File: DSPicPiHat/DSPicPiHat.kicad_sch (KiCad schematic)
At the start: 88 parts, among them J10 Nice!View, J4 Conn_PIC_ICSP_ICD, J5 USB_C_Receptacle_USB2.0, J6 PowerInput, J7 GenericSPIconn, J8 RasPiHeaders, J9 GeneralSPIDisplay, SW1 POWER_Select, SW2 SW_DIP_x08, U1 DSPIC33CH512MP508T-I_PT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

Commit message: Power, USB, and UART
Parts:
- F1: footprint (none) -> Fuse:Fuse_2920_7451Metric
- FB1: footprint (none) -> Resistor_SMD:R_1206_3216Metric
- renumbered Connector_X to Connector_X1, Connector_Y to Connector_Y1, Connector_Z to Connector_Z1
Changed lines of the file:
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@@
     (property "Reference" "F1" (id 0) (at 364.49 186.69 90))
     (property "Value" "3.5 A(?)" (id 1) (at 364.49 189.23 90))
-    (property "Footprint" "" (id 2) (at 369.57 191.77 0)
+    (property "Footprint" "Fuse:Fuse_2920_7451Metric" (id 2) (at 369.57 191.77 0)
       (effects (font (size 1.27 1.27)) (justify left) hide)
     )
@@
   (symbol (lib_id "Connector_Generic:Conn_01x10") (at 92.71 203.2 0) (unit 1)
     (in_bom yes) (on_board yes) (fields_autoplaced)
-    (property "Reference" "Connector_Y" (id 0) (at 95.25 203.1999 0)
+    (property "Reference" "Connector_Y1" (id 0) (at 95.25 203.1999 0)
       (effects (font (size 1.27 1.27)) (justify left))
     )
@@
     (property "Reference" "FB1" (id 0) (at 351.7519 186.69 90))
     (property "Value" "FerriteBead_Small" (id 1) (at 351.7519 189.23 90))
-    (property "Footprint" "" (id 2) (at 351.79 194.818 90)
+    (property "Footprint" "Resistor_SMD:R_1206_3216Metric" (id 2) (at 351.79 194.818 90)
       (effects (font (size 1.27 1.27)) hide)
     )
@@
   (symbol (lib_id "Connector_Generic:Conn_01x10") (at 35.56 203.2 0) (unit 1)
     (in_bom yes) (on_board yes) (fields_autoplaced)
-    (property "Reference" "Connector_X" (id 0) (at 38.1 203.1999 0)
+    (property "Reference" "Connector_X1" (id 0) (at 38.1 203.1999 0)
       (effects (font (size 1.27 1.27)) (justify left))
     )
@@
   (symbol (lib_id "Connector_Generic:Conn_01x10") (at 149.86 203.2 0) (unit 1)
     (in_bom yes) (on_board yes) (fields_autoplaced)
-    (property "Reference" "Connector_Z" (id 0) (at 152.4 203.1999 0)
+    (property "Reference" "Connector_Z1" (id 0) (at 152.4 203.1999 0)
       (effects (font (size 1.27 1.27)) (justify left))
     )
@@
     )
     (path "/a11b1377-8e72-4336-93fb-5d9a6c63e6db"
-      (reference "Connector_X") (unit 1) (value "Conn_01x10") (footprint "Connector_Molex:Molex_Micro-Fit_3.0_43045-1012_2x05_P3.00mm_Vertical")
+      (reference "Connector_X1") (unit 1) (value "Conn_01x10") (footprint "Connector_Molex:Molex_Micro-Fit_3.0_43045-1012_2x05_P3.00mm_Vertical")
     )
     (path "/105a757e-8759-4672-9bee-7cf903751d82"
-      (reference "Connector_Y") (unit 1) (value "Conn_01x10") (footprint "Connector_Molex:Molex_Micro-Fit_3.0_43045-1012_2x05_P3.00mm_Vertical")
+      (reference "Connector_Y1") (unit 1) (value "Conn_01x10") (footprint "Connector_Molex:Molex_Micro-Fit_3.0_43045-1012_2x05_P3.00mm_Vertical")
     )
     (path "/d54e99c0-c1b6-49ce-91c0-733d0cf7acf7"
-      (reference "Connector_Z") (unit 1) (value "Conn_01x10") (footprint "Connector_Molex:Molex_Micro-Fit_3.0_43045-1012_2x05_P3.00mm_Vertical")
+      (reference "Connector_Z1") (unit 1) (value "Conn_01x10") (footprint "Connector_Molex:Molex_Micro-Fit_3.0_43045-1012_2x05_P3.00mm_Vertical")
     )
     (path "/455a802c-8183-4f02-bd06-7b17205bfbf6"
@@
     )
     (path "/0b60c446-5161-421b-a91b-bda5e4f17126"
-      (reference "F1") (unit 1) (value "3.5 A(?)") (footprint "")
+      (reference "F1") (unit 1) (value "3.5 A(?)") (footprint "Fuse:Fuse_2920_7451Metric")
     )
     (path "/73568451-6492-491a-bea8-1d81af82b417"
-      (reference "FB1") (unit 1) (value "FerriteBead_Small") (footprint "")
+      (reference "FB1") (unit 1) (value "FerriteBead_Small") (footprint "Resistor_SMD:R_1206_3216Metric")
     )
     (path "/5662e14b-7d70-457a-a9d1-e3f8a620952f"

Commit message: Connected all the coil driver connectors. Added more footprints.
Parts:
- L1: footprint (none) -> Inductor_SMD:L_0805_2012Metric
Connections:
- net EXT_ADC_X_00: now also U1.5 (RC12); no longer U1.6 (RC13)
- net EXT_ADC_X_01: now also U1.6 (RC13); no longer U1.7 (RC14)
- net EXT_ADC_X_02: now also U1.7 (RC14); no longer U1.8 (RC15)
- net EXT_ADC_X_03: now also U1.8 (RC15); no longer U1.15 (RC0)
- net EXT_ADC_Y_00: now also U1.29 (RC2); no longer U1.41 (RB2)
- net EXT_ADC_Y_01: now also U1.30 (RC6); no longer U1.43 (RB3)
- net EXT_ADC_Y_02: now also U1.33 (RC3); no longer U1.45 (RB4)
- net EXT_ADC_Y_03: now also U1.40 (RC7); no longer U1.46 (RC8)
- net EXT_ADC_Z_00: now also U1.45 (RB4); no longer U1.63 (RC4)
- net EXT_ADC_Z_01: now also U1.46 (RC8); no longer U1.65 (RC5)
- net EXT_ADC_Z_02: now also U1.47 (RC9); no longer U1.66 (RC10)
- net EXT_ADC_Z_03: now also U1.52 (RD7); no longer U1.67 (RC11)
- net EXT_X_PWM_01: now also U1.3 (RB15); no longer U1.74 (RD0)
- net EXT_Y_PWM_00: now also U1.15 (RC0); no longer U1.3 (RB15)
- net EXT_Y_PWM_01: now also U1.28 (RC1); no longer U1.73 (RD1)
- net EXT_Z_PWM_00: now also U1.41 (RB2); no longer U1.5 (RC12)
- net EXT_Z_PWM_01: now also U1.43 (RB3); no longer U1.72 (RD2)

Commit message: PCB mostly routed
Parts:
- removed J10: Nice!View, Connector_PinSocket_2.54mm:PinSocket_1x05_P2.54mm_Vertical, symbol Connector:Conn_01x05_Female
- removed J7: GenericSPIconn, Connector_PinSocket_2.54mm:PinSocket_1x08_P2.54mm_Vertical, symbol Connector:Conn_01x08_Female
- removed J9: GeneralSPIDisplay, Connector_PinSocket_2.54mm:PinSocket_1x08_P2.54mm_Vertical, symbol Connector:Conn_01x08_Female
- added J1: Conn_01x09_Female, Connector_PinHeader_2.54mm:PinHeader_1x09_P2.54mm_Vertical, symbol Connector:Conn_01x09_Female
- C13, C14: footprint Capacitor_SMD:C_0805_2012Metric -> Capacitor_SMD:C_0603_1608Metric
- D12, D13, D4, D5: footprint LED_SMD:LED_WS2812B_PLCC4_5.0x5.0mm_P3.2mm -> LED_SMD:LED_WS2812B-2020_PLCC4_2.0x2.0mm
- JP1: footprint (none) -> Connector_PinHeader_2.54mm:PinHeader_1x02_P2.54mm_Vertical
- Y1: footprint (none) -> Crystal:Crystal_SMD_Abracon_ABM10-4Pin_2.5x2.0mm
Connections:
- net AVSS is gone; now on net GND: C12.2, U1.26 (AVSS)
- net GND1 is gone; now on net GND: C2.2, C4.2, C8.2
- net VDD is gone; now on net +3V3: C10.1, C11.1, C6.1, C9.1, L1.2, U1.12 (VDD), U1.31 (VDD), U1.51 (VDD), U1.71 (VDD)
- net VSS is gone; now on net GND: C10.2, C11.2, C6.2, C9.2, U1.11 (VSS), U1.32 (VSS), U1.50 (VSS), U1.70 (VSS)
- net +3V3: now also J1.1 (Pin_1)
- net Backlight: now also J1.9 (Pin_9)
- net DIP_00: no longer U1.16 (RA0)
- net DIP_01: now also U1.65 (RC5); no longer U1.17 (RE2)
- net DIP_02: now also U1.64 (RE13); no longer U1.18 (RA1)
- net DIP_03: now also U1.63 (RC4); no longer U1.19 (RE3)
- net DIP_04: now also U1.62 (RE12); no longer U1.20 (RA2)
- net DIP_05: now also U1.59 (RE11); no longer U1.21 (RA3)
- net DIP_06: now also U1.58 (RB7); no longer U1.22 (RE4)
- net DIP_07: now also U1.57 (RE10); no longer U1.23 (RA4)
- net Data/Command: now also J1.7 (Pin_7)
- net GND: now also J1.2 (Pin_2)
- net PI_CE0: now also U1.73 (RD1); no longer U1.55 (RB5)
- net PI_CE1: now also J1.6 (Pin_6)
- net PI_MISO: now also U1.74 (RD0), J1.3 (Pin_3); no longer U1.75 (RB10)
- net PI_MOSI: now also U1.75 (RB10), J1.4 (Pin_4); no longer U1.56 (RB6)
- net PI_SCLK: now also J1.5 (Pin_5)
- net RST: now also J1.8 (Pin_8)
- net dsPIC_LED_00: now also U1.19 (RE3); no longer U1.36 (RD11)
- net dsPIC_LED_01: now also U1.18 (RA1); no longer U1.37 (RE6)
- net dsPIC_LED_02: now also U1.17 (RE2); no longer U1.38 (RD10)
- net dsPIC_LED_03: now also U1.16 (RA0); no longer U1.39 (RE7)
- net dsPIC_LED_04: now also U1.14 (RD13); no longer U1.42 (RE8)
- net dsPIC_LED_05: now also U1.13 (RD14); no longer U1.44 (RE9)

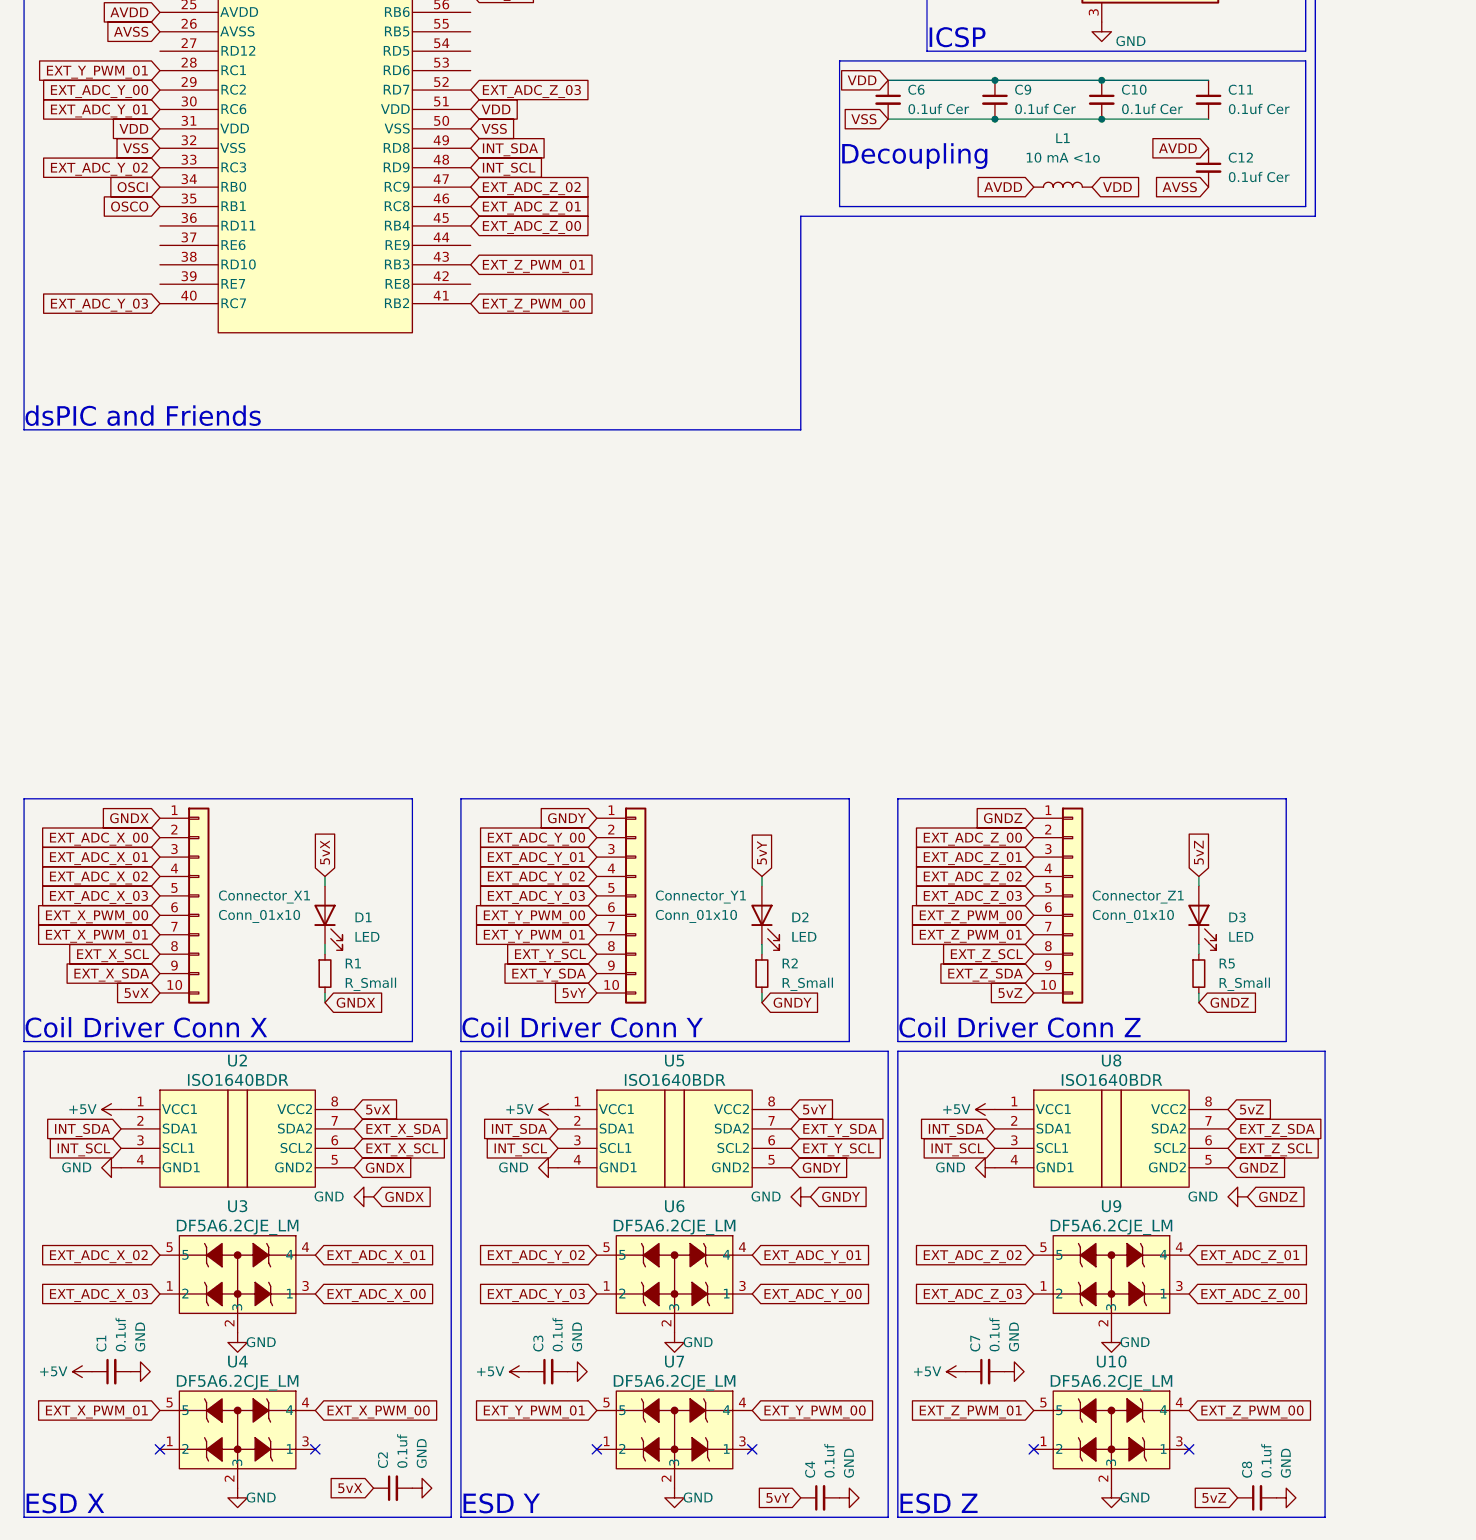
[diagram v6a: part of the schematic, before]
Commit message: changed connectors and removed i2c lines and i2c isolator.
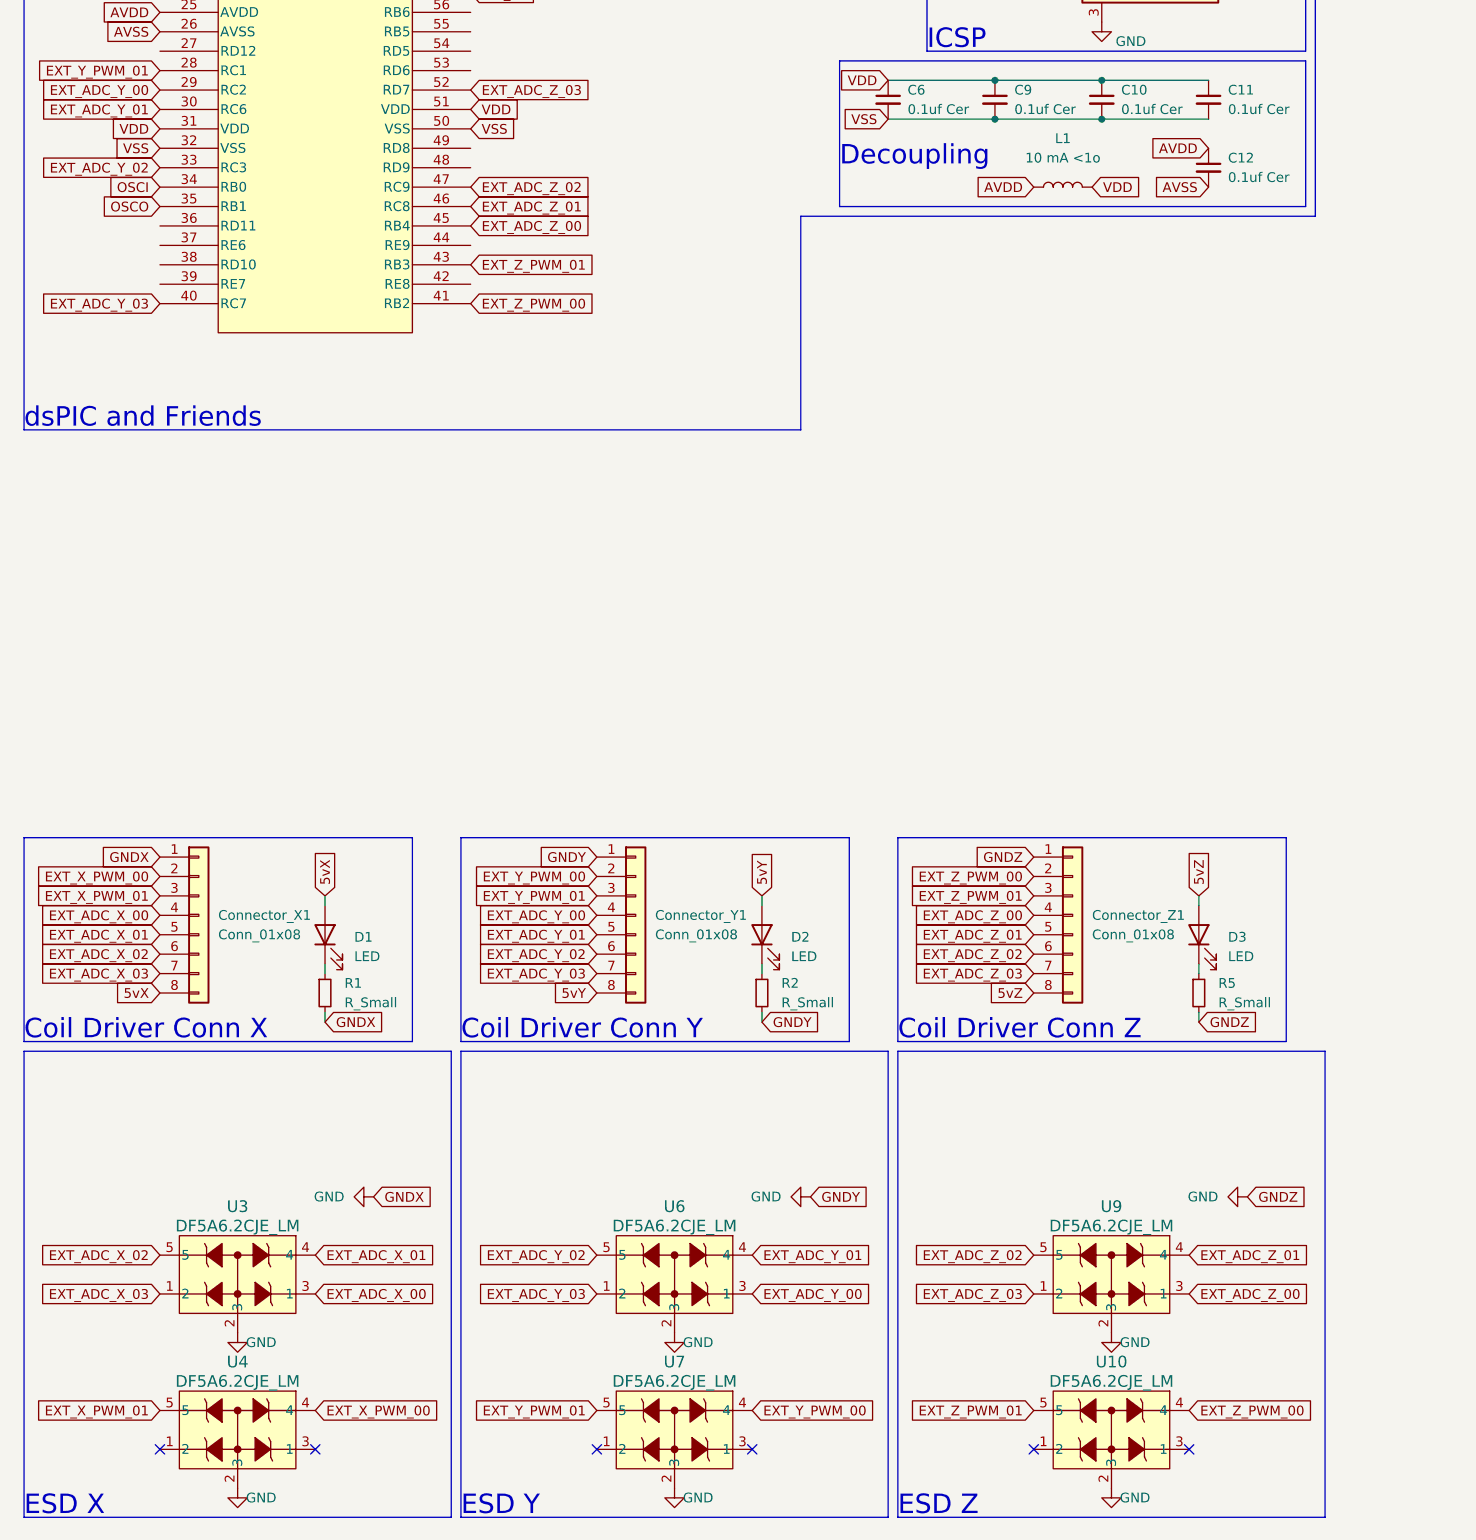
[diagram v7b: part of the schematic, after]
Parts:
- removed C1, C2, C3, C4, C7, C8: 0.1uf, Capacitor_SMD:C_0805_2012Metric, symbol Device:C_Small
- removed Connector_X1, Connector_Y1, Connector_Z1: Conn_01x10, Connector_Molex:Molex_Micro-Fit_3.0_43045-1012_2x05_P3.00mm_Vertical, symbol Connector_Generic:Conn_01x10
- removed U2, U5, U8: ISO1640BDR, Package_SO:SOIC-8-1EP_3.9x4.9mm_P1.27mm_EP2.29x3mm, symbol PiHatLib:ISO1640BDR
- added Connector_X1, Connector_Y1, Connector_Z1: Conn_01x08, Connector_Molex:Molex_Pico-Clasp_202396-0807_1x08-1MP_P1.00mm_Horizontal, symbol Connector_Generic:Conn_01x08
- J6: footprint Connector_Molex:Molex_Micro-Fit_3.0_43045-0212_2x01_P3.00mm_Vertical -> Connector_Molex:Molex_Pico-Clasp_202396-0207_1x02-1MP_P1.00mm_Horizontal
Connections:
- net 5vX: now also Connector_X1.8 (Pin_8)
- net 5vY: now also Connector_Y1.8 (Pin_8)
- net 5vZ: now also Connector_Z1.8 (Pin_8)
- net EXT_ADC_X_00: now also Connector_X1.4 (Pin_4)
- net EXT_ADC_X_01: now also Connector_X1.5 (Pin_5)
- net EXT_ADC_X_02: now also Connector_X1.6 (Pin_6)
- net EXT_ADC_X_03: now also Connector_X1.7 (Pin_7)
- net EXT_ADC_Y_00: now also Connector_Y1.4 (Pin_4)
- net EXT_ADC_Y_01: now also Connector_Y1.5 (Pin_5)
- net EXT_ADC_Y_02: now also Connector_Y1.6 (Pin_6)
- net EXT_ADC_Y_03: now also Connector_Y1.7 (Pin_7)
- net EXT_ADC_Z_00: now also Connector_Z1.4 (Pin_4)
- net EXT_ADC_Z_01: now also Connector_Z1.5 (Pin_5)
- net EXT_ADC_Z_02: now also Connector_Z1.6 (Pin_6)
- net EXT_ADC_Z_03: now also Connector_Z1.7 (Pin_7)
- net EXT_X_PWM_00: now also Connector_X1.2 (Pin_2)
- net EXT_X_PWM_01: now also Connector_X1.3 (Pin_3)
- net EXT_Y_PWM_00: now also Connector_Y1.2 (Pin_2)
- net EXT_Y_PWM_01: now also Connector_Y1.3 (Pin_3)
- net EXT_Z_PWM_00: now also Connector_Z1.2 (Pin_2)
- net EXT_Z_PWM_01: now also Connector_Z1.3 (Pin_3)
- net GND: now also Connector_X1.1 (Pin_1), Connector_Y1.1 (Pin_1), Connector_Z1.1 (Pin_1)
- net INT_SCL: no longer names the net of U1.48 (RD9)
- net INT_SDA: no longer names the net of U1.49 (RD8)
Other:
- moved on the sheet: D1, D2, D3, R1, R2, R5
